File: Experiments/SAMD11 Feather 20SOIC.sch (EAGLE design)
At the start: 30 parts, among them IC1 ATSAMD11D14A-SSNT, J1 10118193-0001LF, Q1 DMG341, SW1 SPST_TACT-KMR2, U1 AP2112-3.3, U2 MCP73831T-2ACI/OT, X1 JSTPH, X2 2x5 0.05" SWD

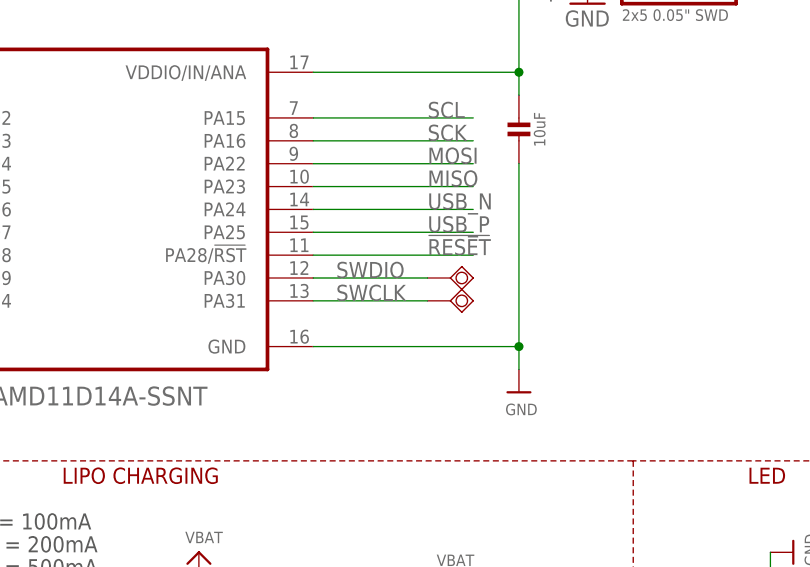
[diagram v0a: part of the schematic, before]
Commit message: unswap swdio and swclk pins
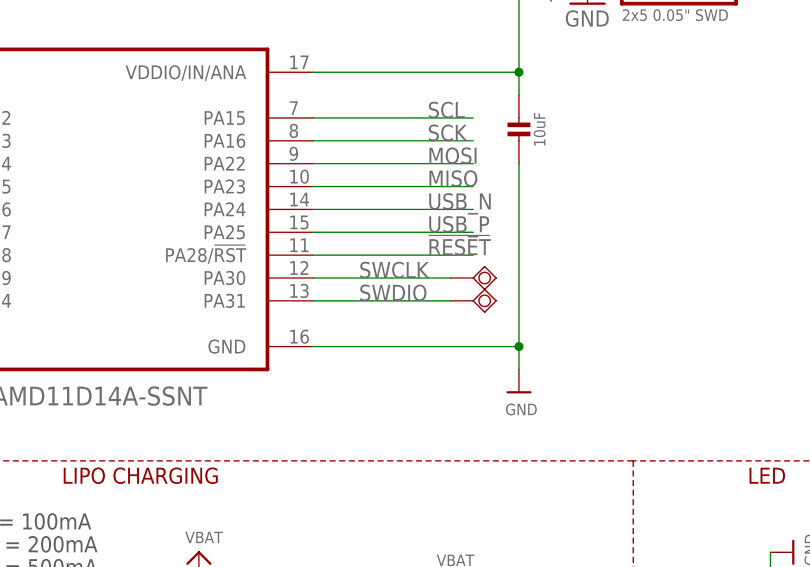
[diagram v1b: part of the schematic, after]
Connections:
- net SWCLK: now also IC1.PA30; no longer IC1.PA31
- net SWDIO: now also IC1.PA31; no longer IC1.PA30
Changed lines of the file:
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@@
 <attribute name="VALUE" x="92.456" y="53.34" size="1.27" layer="96"/>
 </instance>
-<instance part="SWCLK" gate="G$1" x="86.36" y="66.04" smashed="yes" rot="R90">
-<attribute name="TP_SIGNAL_NAME" x="87.63" y="68.58" size="1.778" layer="97" rot="R90"/>
-</instance>
-<instance part="SWDIO" gate="G$1" x="86.36" y="68.58" smashed="yes" rot="R90">
-<attribute name="TP_SIGNAL_NAME" x="87.63" y="71.12" size="1.778" layer="97" rot="R90"/>
+<instance part="SWCLK" gate="G$1" x="88.9" y="68.58" smashed="yes" rot="R90">
+<attribute name="TP_SIGNAL_NAME" x="90.17" y="71.12" size="1.778" layer="97" rot="R90"/>
+</instance>
+<instance part="SWDIO" gate="G$1" x="88.9" y="66.04" smashed="yes" rot="R90">
+<attribute name="TP_SIGNAL_NAME" x="90.17" y="68.58" size="1.778" layer="97" rot="R90"/>
 </instance>
 <instance part="FRAME1" gate="G$1" x="0" y="0" smashed="yes">
@@
 <net name="SWDIO" class="0">
 <segment>
-<wire x1="71.12" y1="68.58" x2="83.82" y2="68.58" width="0.1524" layer="91"/>
 <pinref part="SWDIO" gate="G$1" pin="TP"/>
-<pinref part="IC1" gate="G$1" pin="PA30"/>
-<label x="73.66" y="68.58" size="1.778" layer="95"/>
+<wire x1="71.12" y1="66.04" x2="86.36" y2="66.04" width="0.1524" layer="91"/>
+<label x="76.2" y="66.04" size="1.778" layer="95"/>
+<pinref part="IC1" gate="G$1" pin="PA31"/>
 </segment>
 <segment>
@@
 <net name="SWCLK" class="0">
 <segment>
-<wire x1="71.12" y1="66.04" x2="83.82" y2="66.04" width="0.1524" layer="91"/>
 <pinref part="SWCLK" gate="G$1" pin="TP"/>
-<pinref part="IC1" gate="G$1" pin="PA31"/>
-<label x="73.66" y="66.04" size="1.778" layer="95"/>
-</segment>
-<segment>
+<wire x1="71.12" y1="68.58" x2="86.36" y2="68.58" width="0.1524" layer="91"/>
+<label x="76.2" y="68.58" size="1.778" layer="95"/>
+<pinref part="IC1" gate="G$1" pin="PA30"/>
+</segment>
+<segment>

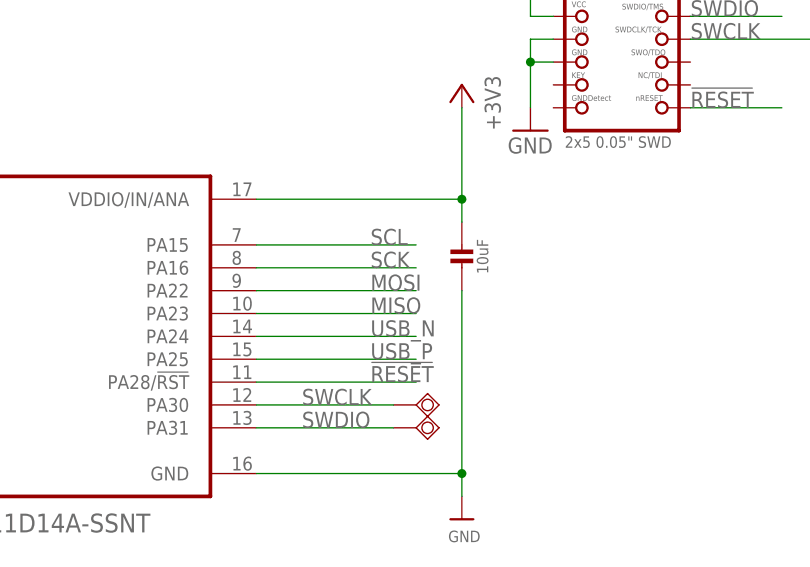
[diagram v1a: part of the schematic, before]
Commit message: fix SPI pin muxing
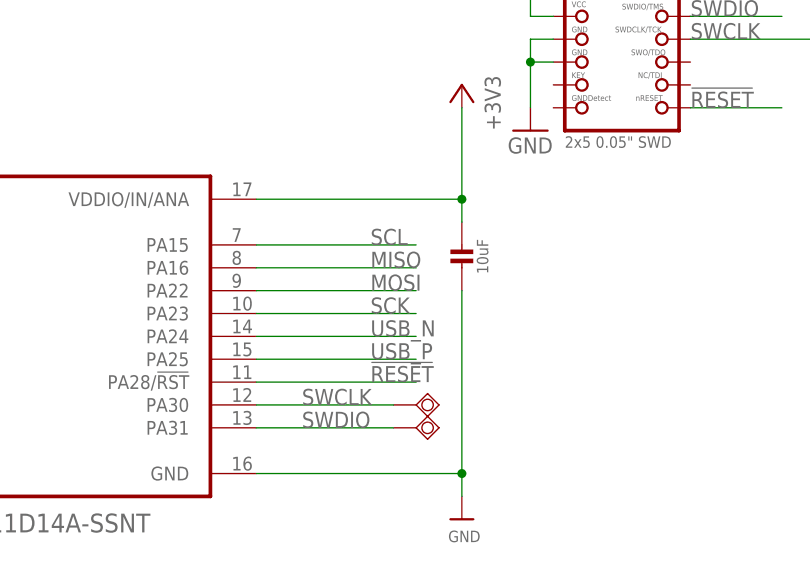
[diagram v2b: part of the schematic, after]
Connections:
- net MISO: now also IC1.PA16; no longer IC1.PA23
- net SCK: now also IC1.PA23; no longer IC1.PA16
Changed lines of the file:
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@@
 </segment>
 <segment>
-<pinref part="IC1" gate="G$1" pin="PA23"/>
-<wire x1="71.12" y1="78.74" x2="88.9" y2="78.74" width="0.1524" layer="91"/>
-<label x="83.82" y="78.74" size="1.778" layer="95"/>
+<pinref part="IC1" gate="G$1" pin="PA16"/>
+<wire x1="71.12" y1="83.82" x2="88.9" y2="83.82" width="0.1524" layer="91"/>
+<label x="83.82" y="83.82" size="1.778" layer="95"/>
 </segment>
 </net>
@@
 </segment>
 <segment>
-<pinref part="IC1" gate="G$1" pin="PA16"/>
-<wire x1="71.12" y1="83.82" x2="88.9" y2="83.82" width="0.1524" layer="91"/>
-<label x="83.82" y="83.82" size="1.778" layer="95"/>
+<pinref part="IC1" gate="G$1" pin="PA23"/>
+<wire x1="71.12" y1="78.74" x2="88.9" y2="78.74" width="0.1524" layer="91"/>
+<label x="83.82" y="78.74" size="1.778" layer="95"/>
 </segment>
 </net>
